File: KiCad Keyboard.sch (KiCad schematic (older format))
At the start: 93 parts, among them U1 TEENSY2.0

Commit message: Add row/column labels
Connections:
- net labels added: Column0, Column1, Column2, Column3, Column4, Column5, Column6, Column7, Column8, Row0, Row1, Row2, Row3, Row4, Row5
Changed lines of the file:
@@
 Wire Wire Line
 	9800 1750 9800 5700
+Text Label 11650 3800 0    60   ~ 0
+Row0
+Text Label 2800 1300 0    60   ~ 0
+Row0
+Text Label 2800 2050 0    60   ~ 0
+Row1
+Text Label 2800 2800 0    60   ~ 0
+Row2
+Text Label 2800 3550 0    60   ~ 0
+Row3
+Text Label 2800 4300 0    60   ~ 0
+Row4
+Text Label 2800 5050 0    60   ~ 0
+Row5
+Text Label 3000 5700 3    60   ~ 0
+Column0
+Text Label 3850 5700 3    60   ~ 0
+Column1
+Text Label 4700 5700 3    60   ~ 0
+Column2
+Text Label 5550 5700 3    60   ~ 0
+Column3
+Text Label 6400 5700 3    60   ~ 0
+Column4
+Text Label 7250 5700 3    60   ~ 0
+Column5
+Text Label 8100 5700 3    60   ~ 0
+Column6
+Text Label 8950 5700 3    60   ~ 0
+Column7
+Text Label 9800 5700 3    60   ~ 0
+Column8
 $EndSCHEMATC

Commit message: Wire row/column to teensy
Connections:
- net Column0: now also U1.22 (PB6)
- net Column1: now also U1.6 (PB7)
- net Column2: now also U1.11 (PC6)
- net Column3: now also U1.12 (PC7)
- net Column4: now also U1.7 (PD0)
- net Column5: now also U1.8 (PD1)
- net Column6: now also U1.9 (PD2)
- net Column7: now also U1.10 (PD3)
- net Column8: now also U1.17 (PD4)
- net Row0: now also U1.2 (PB0)
- net Row1: now also U1.3 (PB1)
- net Row2: now also U1.4 (PB2)
- net Row3: now also U1.5 (PB3)
- net Row4: now also U1.20 (PB4)
- net Row5: now also U1.21 (PB5)
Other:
- moved on the sheet: D_1, D_2, D_3, D_4, D_5, D_6, D_A, D_B, D_C, D_D, D_E, D_Esc_0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

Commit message: Stray row label
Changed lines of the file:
@@
 LIBS:contrib
 LIBS:valves
-LIBS:ergodox
-LIBS:BathroomEpiphanies
 LIBS:KiCad Keyboard-cache
 EELAYER 25 0
@@
 	1    0    0    -1
 $EndComp
-Text Label 11650 3800 0    60   ~ 0
-Row0
 Text Label 3350 1350 0    60   ~ 0
 Row0
@@
 Connection ~ 9600 5100
 Wire Wire Line
-	10450 1350 3350 1350
-Wire Wire Line
-	3300 2100 10450 2100
-Wire Wire Line
-	3250 2850 9600 2850
-Wire Wire Line
-	3200 3600 9600 3600
-Wire Wire Line
-	3150 4350 9600 4350
-Wire Wire Line
-	3100 5100 9600 5100
-Wire Wire Line
-	3550 2550 3550 5750
-Wire Wire Line
-	4400 2550 4400 5800
-Wire Wire Line
-	5250 1800 5250 5900
-Wire Wire Line
-	6100 1800 6100 6000
-Wire Wire Line
-	6950 1800 6950 6050
-Wire Wire Line
-	7800 1800 7800 6150
-Wire Wire Line
-	8650 1800 8650 6200
-Wire Wire Line
-	9500 1800 9500 6250
-Wire Wire Line
-	10350 1800 10350 6300
+	10450 1350 9600 1350
+Wire Wire Line
+	9600 1350 8750 1350
+Wire Wire Line
+	8750 1350 7900 1350
+Wire Wire Line
+	7900 1350 7050 1350
+Wire Wire Line
+	7050 1350 6200 1350
+Wire Wire Line
+	6200 1350 5350 1350
+Wire Wire Line
+	5350 1350 3350 1350
+Wire Wire Line
+	3300 2100 3650 2100
+Wire Wire Line
+	3650 2100 4500 2100
+Wire Wire Line
+	4500 2100 5350 2100
+Wire Wire Line
+	5350 2100 6200 2100
+Wire Wire Line
+	6200 2100 7050 2100
+Wire Wire Line
+	7050 2100 7900 2100
+Wire Wire Line
+	7900 2100 8750 2100
+Wire Wire Line
+	8750 2100 9600 2100
+Wire Wire Line
+	9600 2100 10450 2100
+Wire Wire Line
+	3250 2850 3650 2850
+Wire Wire Line
+	3650 2850 4500 2850
+Wire Wire Line
+	4500 2850 5350 2850
+Wire Wire Line
+	5350 2850 6200 2850
+Wire Wire Line
+	6200 2850 7050 2850
+Wire Wire Line
+	7050 2850 7900 2850
+Wire Wire Line
+	7900 2850 8750 2850
+Wire Wire Line
+	8750 2850 9600 2850
+Wire Wire Line
+	3200 3600 3650 3600
+Wire Wire Line
+	3650 3600 4500 3600
+Wire Wire Line
+	4500 3600 5350 3600
+Wire Wire Line
+	5350 3600 6200 3600
+Wire Wire Line
+	6200 3600 7050 3600
+Wire Wire Line
+	7050 3600 7900 3600
+Wire Wire Line
+	7900 3600 8750 3600
+Wire Wire Line
+	8750 3600 9600 3600
+Wire Wire Line
+	3150 4350 3650 4350
+Wire Wire Line
+	3650 4350 4500 4350
+Wire Wire Line
+	4500 4350 5350 4350
+Wire Wire Line
+	5350 4350 6200 4350
+Wire Wire Line
+	6200 4350 7050 4350
+Wire Wire Line
+	7050 4350 7900 4350
+Wire Wire Line
+	7900 4350 8750 4350
+Wire Wire Line
+	8750 4350 9600 4350
+Wire Wire Line
+	3100 5100 3650 5100
+Wire Wire Line
+	3650 5100 4500 5100
+Wire Wire Line
+	4500 5100 5350 5100
+Wire Wire Line
+	5350 5100 6200 5100
+Wire Wire Line
+	6200 5100 7050 5100
+Wire Wire Line
+	7050 5100 9600 5100
+Wire Wire Line
+	3550 2550 3550 3300
+Wire Wire Line
+	3550 3300 3550 4050
+Wire Wire Line
+	3550 4050 3550 4800
+Wire Wire Line
+	3550 4800 3550 5550
+Wire Wire Line
+	3550 5550 3550 5750
+Wire Wire Line
+	4400 2550 4400 3300
+Wire Wire Line
+	4400 3300 4400 4050
+Wire Wire Line
+	4400 4050 4400 4800
+Wire Wire Line
+	4400 4800 4400 5550
+Wire Wire Line
+	4400 5550 4400 5800
+Wire Wire Line
+	5250 1800 5250 2550
+Wire Wire Line
+	5250 2550 5250 3300
+Wire Wire Line
+	5250 3300 5250 4050
+Wire Wire Line
+	5250 4050 5250 4800
+Wire Wire Line
+	5250 4800 5250 5550
+Wire Wire Line
+	5250 5550 5250 5900
+Wire Wire Line
+	6100 1800 6100 2550
+Wire Wire Line
+	6100 2550 6100 3300
+Wire Wire Line
+	6100 3300 6100 4050
+Wire Wire Line
+	6100 4050 6100 4800
+Wire Wire Line
+	6100 4800 6100 5550
+Wire Wire Line
+	6100 5550 6100 6000
+Wire Wire Line
+	6950 1800 6950 2550
+Wire Wire Line
+	6950 2550 6950 3300
+Wire Wire Line
+	6950 3300 6950 4050
+Wire Wire Line
+	6950 4050 6950 4800
+Wire Wire Line
+	6950 4800 6950 5550
+Wire Wire Line
+	6950 5550 6950 6050
+Wire Wire Line
+	7800 1800 7800 2550
+Wire Wire Line
+	7800 2550 7800 3300
+Wire Wire Line
+	7800 3300 7800 4050
+Wire Wire Line
+	7800 4050 7800 4800
+Wire Wire Line
+	7800 4800 7800 6150
+Wire Wire Line
+	8650 1800 8650 2550
+Wire Wire Line
+	8650 2550 8650 3300
+Wire Wire Line
+	8650 3300 8650 4050
+Wire Wire Line
+	8650 4050 8650 4800
+Wire Wire Line
+	8650 4800 8650 6200
+Wire Wire Line
+	9500 1800 9500 2550
+Wire Wire Line
+	9500 2550 9500 3300
+Wire Wire Line
+	9500 3300 9500 4050
+Wire Wire Line
+	9500 4050 9500 4800
+Wire Wire Line
+	9500 4800 9500 5550
+Wire Wire Line
+	9500 5550 9500 6250
+Wire Wire Line
+	10350 1800 10350 2550
+Wire Wire Line
+	10350 2550 10350 6300
 Wire Wire Line
 	3350 1350 3350 750

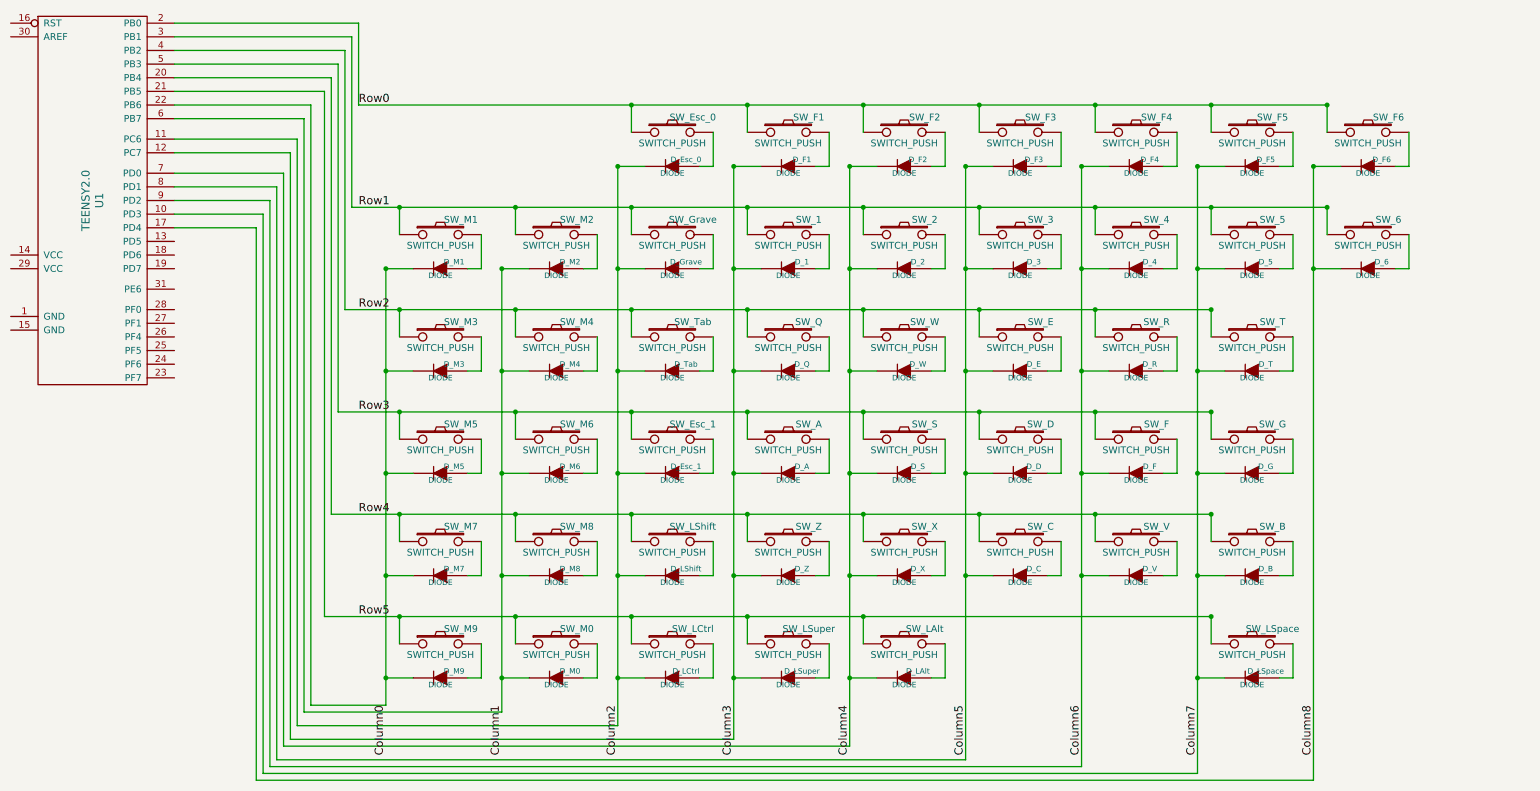
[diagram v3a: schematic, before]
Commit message: Changing diodes to SMD
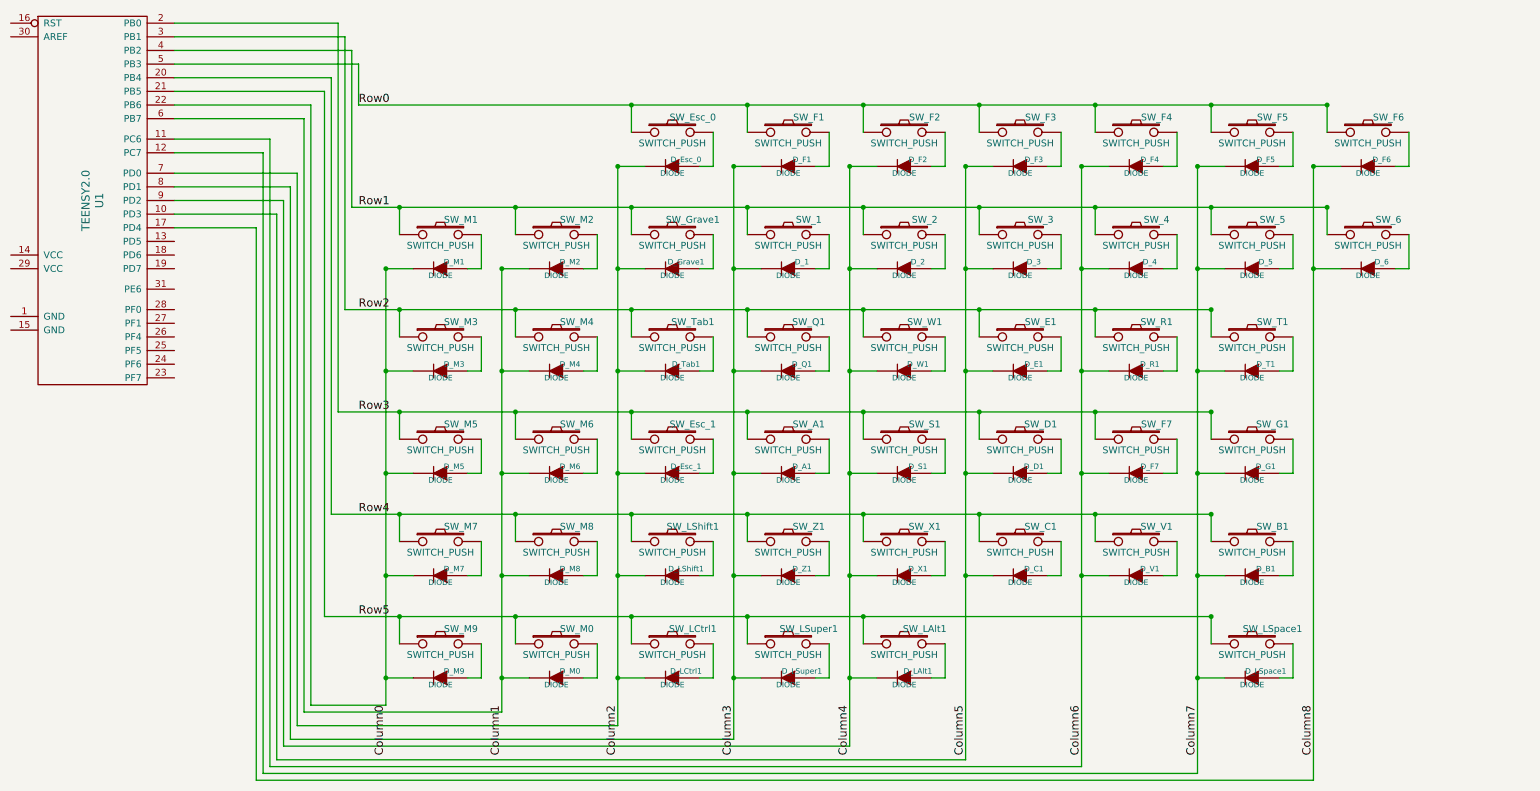
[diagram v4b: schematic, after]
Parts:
- renumbered D_A to D_A1, D_B to D_B1, D_C to D_C1, D_D to D_D1, D_E to D_E1, D_F to D_F7, D_G to D_G1, D_Grave to D_Grave1, D_LAlt to D_LAlt1, D_LCtrl to D_LCtrl1, D_LShift to D_LShift1, D_LSpace to D_LSpace1, D_LSuper to D_LSuper1, D_Q to D_Q1, D_R to D_R1, D_S to D_S1, D_T to D_T1, D_Tab to D_Tab1, D_V to D_V1, D_W to D_W1, D_X to D_X1, D_Z to D_Z1, SW_A to SW_A1, SW_B to SW_B1, SW_C to SW_C1, SW_D to SW_D1, SW_E to SW_E1, SW_F to SW_F7, SW_G to SW_G1, SW_Grave to SW_Grave1, SW_LAlt to SW_LAlt1, SW_LCtrl to SW_LCtrl1, SW_LShift to SW_LShift1, SW_LSpace to SW_LSpace1, SW_LSuper to SW_LSuper1, SW_Q to SW_Q1, SW_R to SW_R1, SW_S to SW_S1, SW_T to SW_T1, SW_Tab to SW_Tab1, SW_V to SW_V1, SW_W to SW_W1, SW_X to SW_X1, SW_Z to SW_Z1
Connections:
- net Column2: now also U1.7 (PD0); no longer U1.11 (PC6)
- net Column3: now also U1.8 (PD1); no longer U1.12 (PC7)
- net Column4: now also U1.9 (PD2); no longer U1.7 (PD0)
- net Column5: now also U1.10 (PD3); no longer U1.8 (PD1)
- net Column6: now also U1.11 (PC6); no longer U1.9 (PD2)
- net Column7: now also U1.12 (PC7); no longer U1.10 (PD3)
- net Row0: now also U1.5 (PB3); no longer U1.2 (PB0)
- net Row1: now also U1.4 (PB2); no longer U1.3 (PB1)
- net Row2: now also U1.3 (PB1); no longer U1.4 (PB2)
- net Row3: now also U1.2 (PB0); no longer U1.5 (PB3)
